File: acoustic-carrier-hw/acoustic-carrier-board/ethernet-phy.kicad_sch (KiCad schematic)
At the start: 51 parts, among them J1201 HR911130A, U1201 KSZ9031RN, Y1201 25MHz

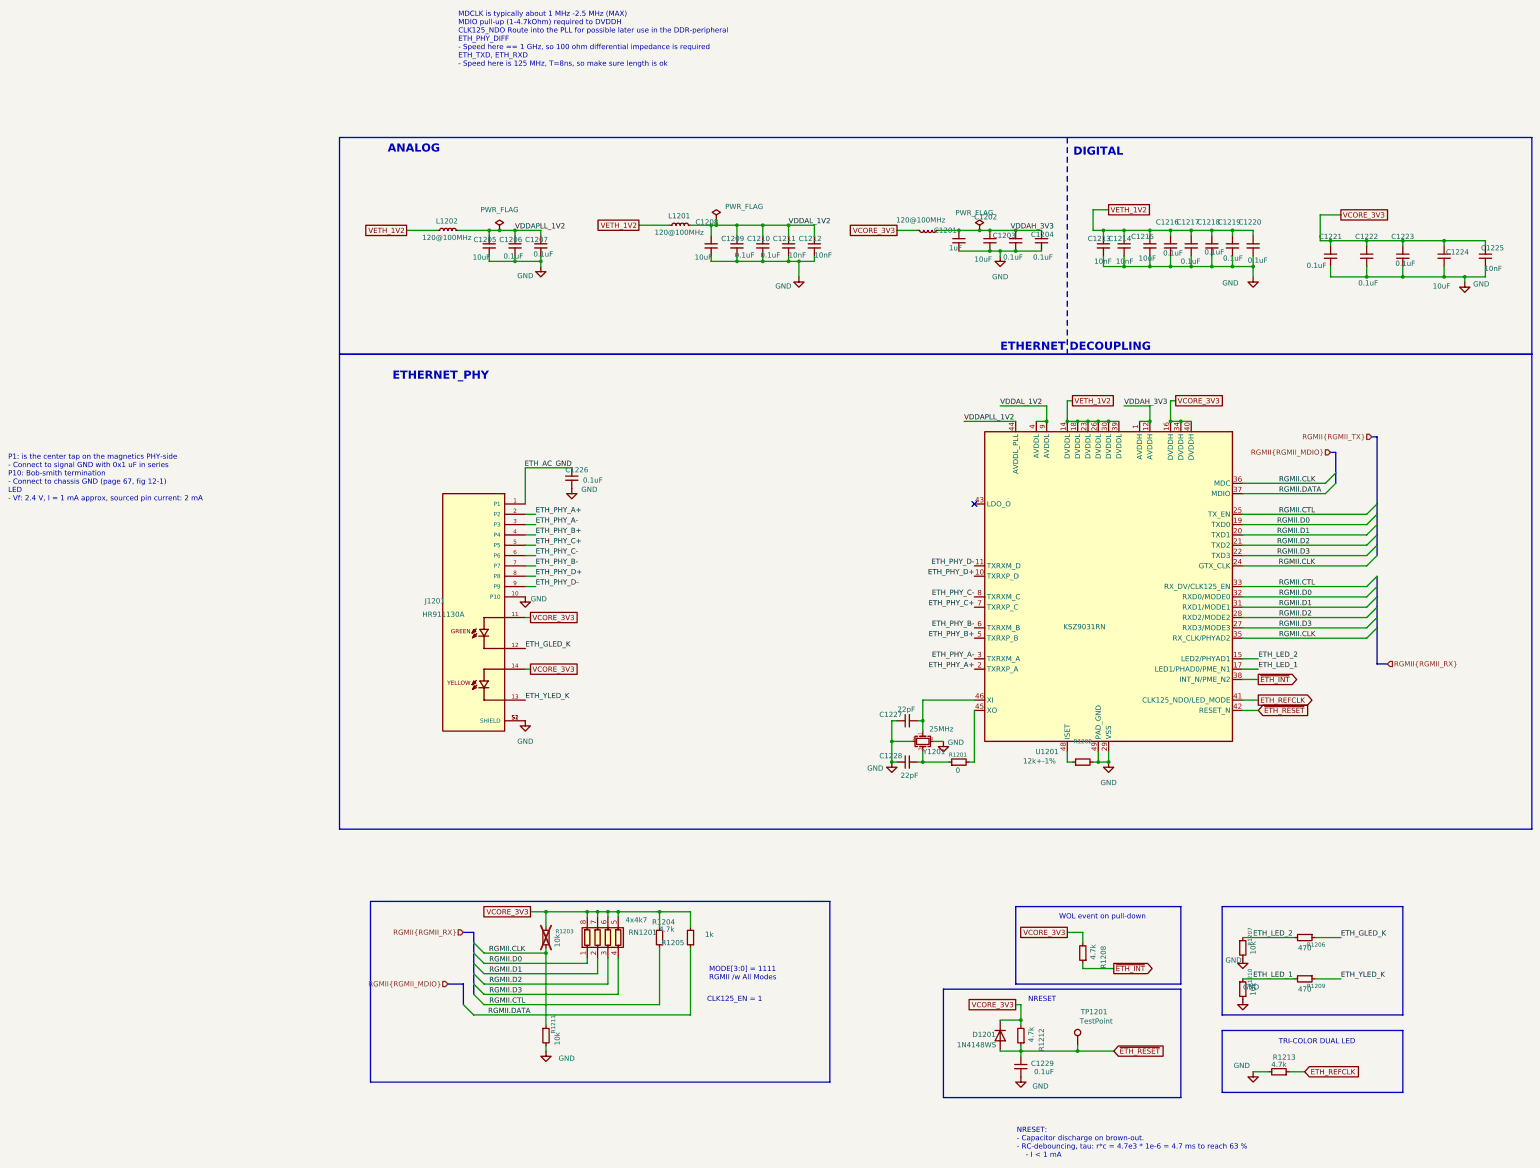
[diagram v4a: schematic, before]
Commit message: [carrier] Removed USB-switch, placed decouplpling for DDR3 and ECP5U (next) consider adding buffers on CC1 and CC2 pins
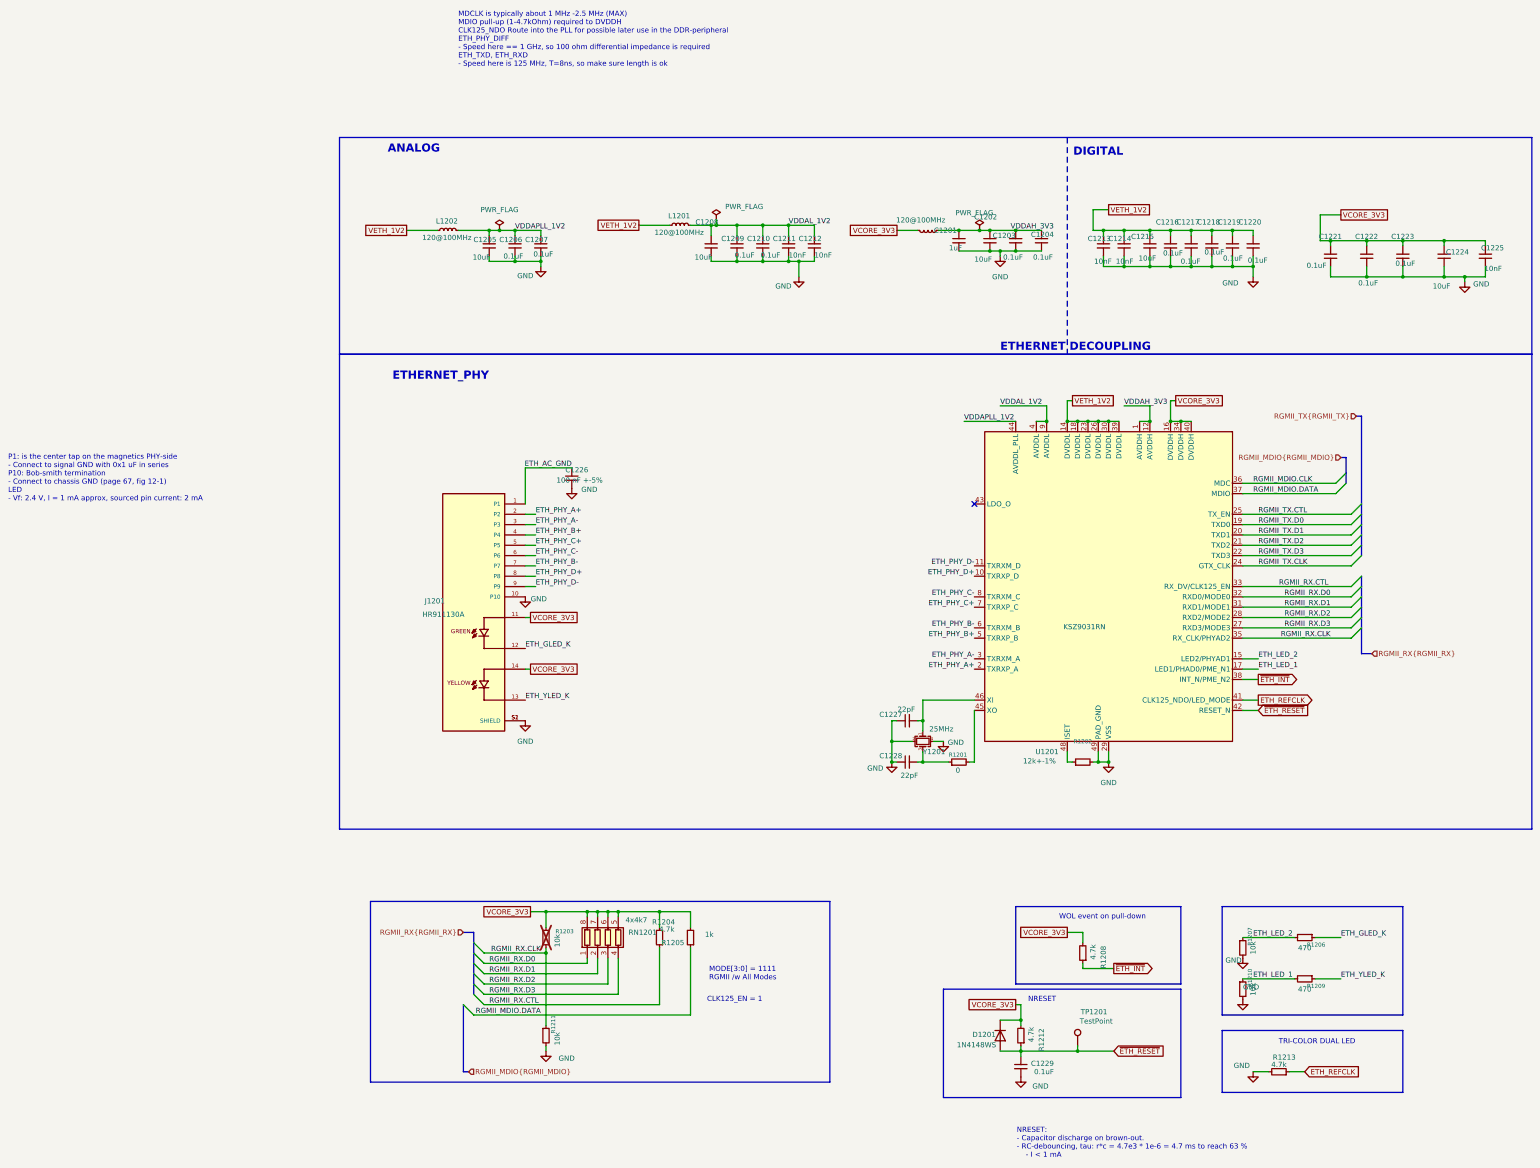
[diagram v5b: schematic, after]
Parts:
- C1203, C1204, C1206, C1207, C1209, C1210, C1216, C1217, C1218, C1219, C1220, C1221, C1222, C1223, C1229: footprint Capacitor_SMD:C_0402_1005Metric -> Capacitor_SMD:C_0201_0603Metric; LPN C307331 -> C22435929; MPN CL05B104KB54PNC -> CGA0201X7R104K160ET
- C1211, C1212, C1213, C1214, C1225: footprint Capacitor_SMD:C_0402_1005Metric -> Capacitor_SMD:C_0201_0603Metric; LPN C15195 -> C285010; MPN CL05B103KB5NNNC -> 0201B103K250NT
- C1226: value 0.1uF -> 100 nF +-5%
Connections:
- net RGMII.CLK renamed RGMII_RX.CLK
- net RGMII_RX.CLK: no longer U1201.24 (GTX_CLK), U1201.36 (MDC)
- net RGMII.CTL renamed RGMII_RX.CTL
- net RGMII_RX.CTL: no longer U1201.25 (TX_EN)
- net RGMII.D0 renamed RGMII_RX.D0
- net RGMII_RX.D0: no longer U1201.19 (TXD0)
- net RGMII.D1 renamed RGMII_RX.D1
- net RGMII_RX.D1: no longer U1201.20 (TXD1)
- net RGMII.D2 renamed RGMII_RX.D2
- net RGMII_RX.D2: no longer U1201.21 (TXD2)
- net RGMII.D3 renamed RGMII_RX.D3
- net RGMII_RX.D3: no longer U1201.22 (TXD3)
- net RGMII.DATA renamed RGMII_MDIO.DATA
- new net RGMII_MDIO.CLK: U1201.36 (MDC)
- new net RGMII_TX.CLK: U1201.24 (GTX_CLK)
- new net RGMII_TX.CTL: U1201.25 (TX_EN)
- new net RGMII_TX.D0: U1201.19 (TXD0)
- new net RGMII_TX.D1: U1201.20 (TXD1)
- new net RGMII_TX.D2: U1201.21 (TXD2)
- new net RGMII_TX.D3: U1201.22 (TXD3)

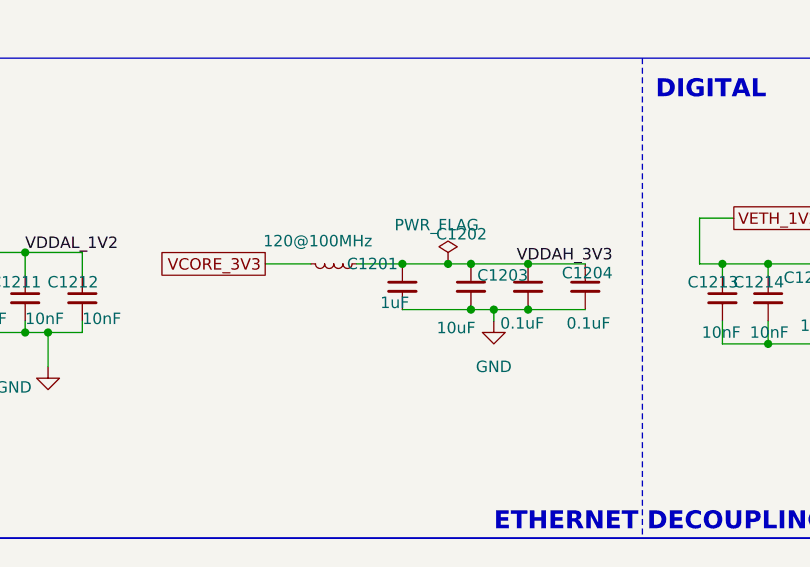
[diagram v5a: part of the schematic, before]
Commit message: [carrier] connected ethernet, usb and adc to appropriate banks, redpositioned schmitt trigger and USB
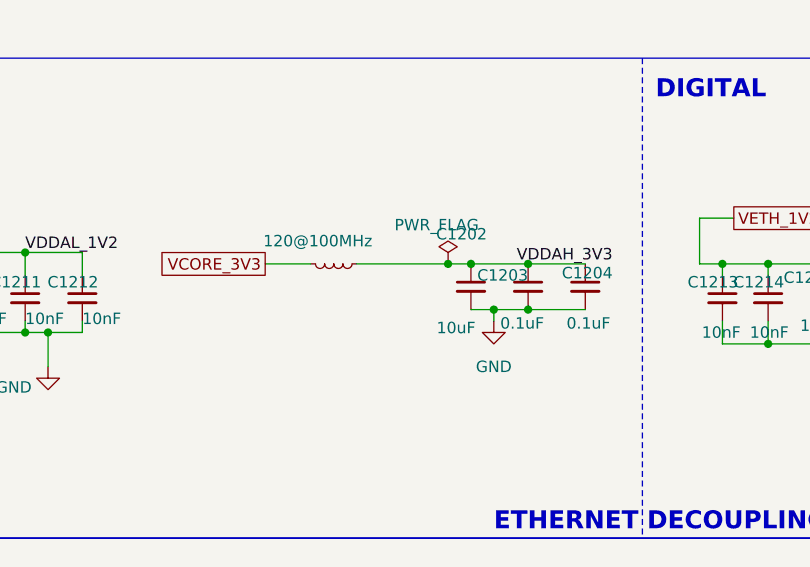
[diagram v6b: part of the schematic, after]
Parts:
- removed C1201: 1uF, Capacitor_SMD:C_0805_2012Metric, symbol Device:C_Small

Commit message: [carrier] Layout more or less complete (next) think about adding 6x2 connectors, and add extra pin signals to the connector for testing
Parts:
- R1205: footprint Resistor_SMD:R_0805_2012Metric_Pad1.20x1.40mm_HandSolder -> Resistor_SMD:R_0402_1005Metric; LPN C17513 -> C11702; MPN 0805W8F1001T5E -> 0402WGF1001TCE
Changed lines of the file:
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@@
 			)
 		)
-		(property "Footprint" "Resistor_SMD:R_0805_2012Metric_Pad1.20x1.40mm_HandSolder"
+		(property "Footprint" "Resistor_SMD:R_0402_1005Metric"
 			(at 107.95 219.71 0)
 			(effects
@@
 			)
 		)
-		(property "MPN" "0805W8F1001T5E"
+		(property "MPN" "0402WGF1001TCE"
 			(at 107.95 219.71 0)
 			(effects
@@
 			)
 		)
-		(property "LPN" "C17513"
+		(property "LPN" "C11702"
 			(at 107.95 219.71 0)
 			(effects
